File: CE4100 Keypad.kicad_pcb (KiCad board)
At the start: 2 copper layers, 114 x 152 mm, 54 parts, among them J1 USB_C, J2 AVR-ISP, J3 GU112X16G-7003, SW1 RESET, SW10 Key_1, SW11 Key_0, SW12 Key_Slash, SW13 Key_8, SW14 Key_5, SW15 Key_2, SW16 Key_Star, SW17 Key_9, SW18 Key_6, SW19 Key_3, SW2 Key_M1, SW20 Key_Del, SW21 Key_Minus, SW22 Key_Plus, SW23 Rotary_Switch, SW24 Key_Return, SW25 Rotary_Switch, SW3 Key_M2, SW4 Key_M3, SW5 Key_M4, SW6 Key_M5, SW7 Key_NumLock, SW8 Key_7, SW9 Key_4, U1 ATmega32U4

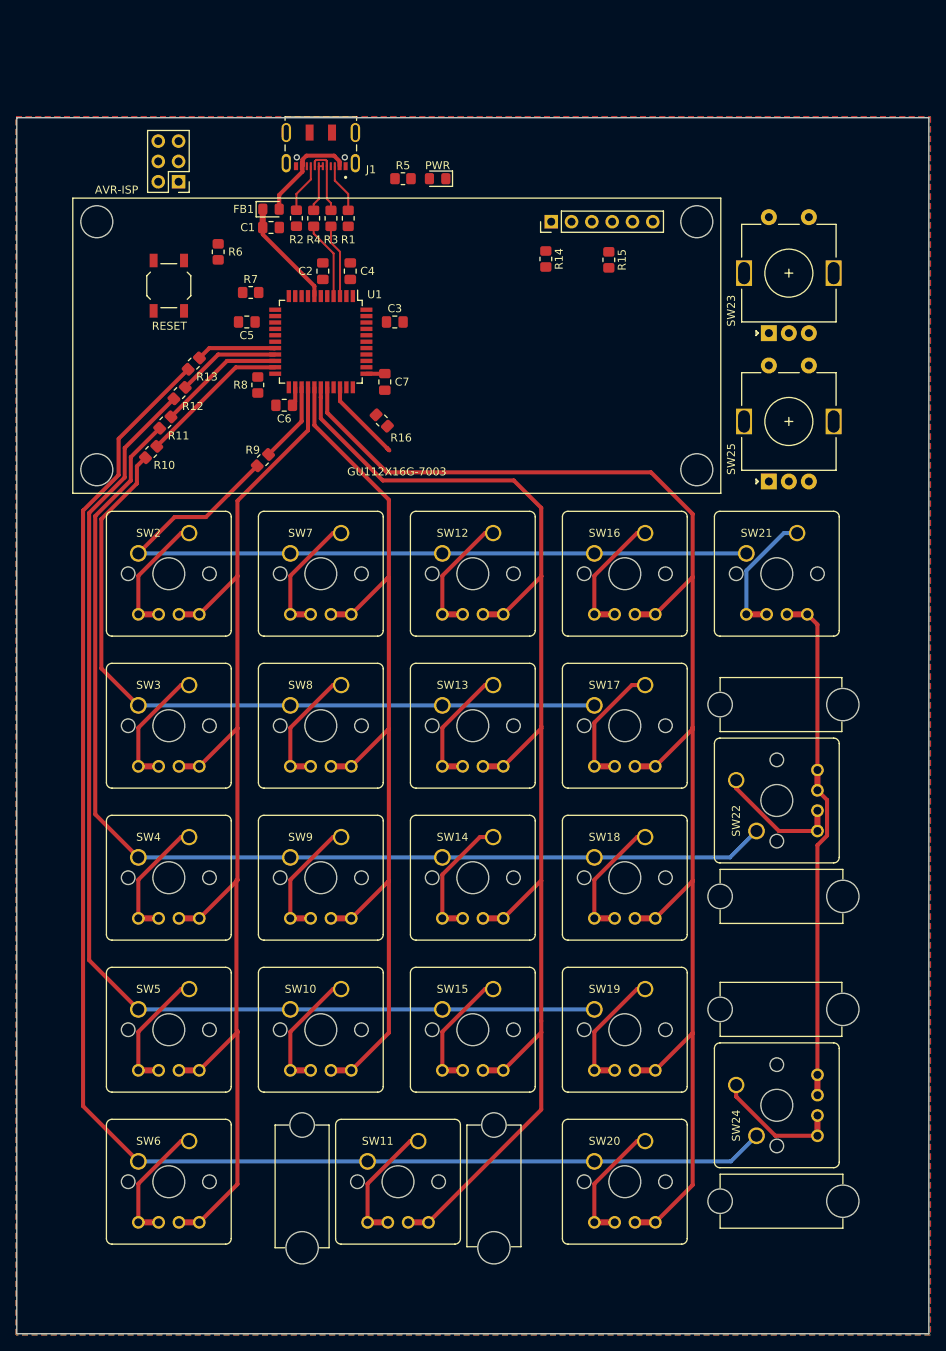
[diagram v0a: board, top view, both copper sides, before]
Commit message: Added more 3D models and worked on layout
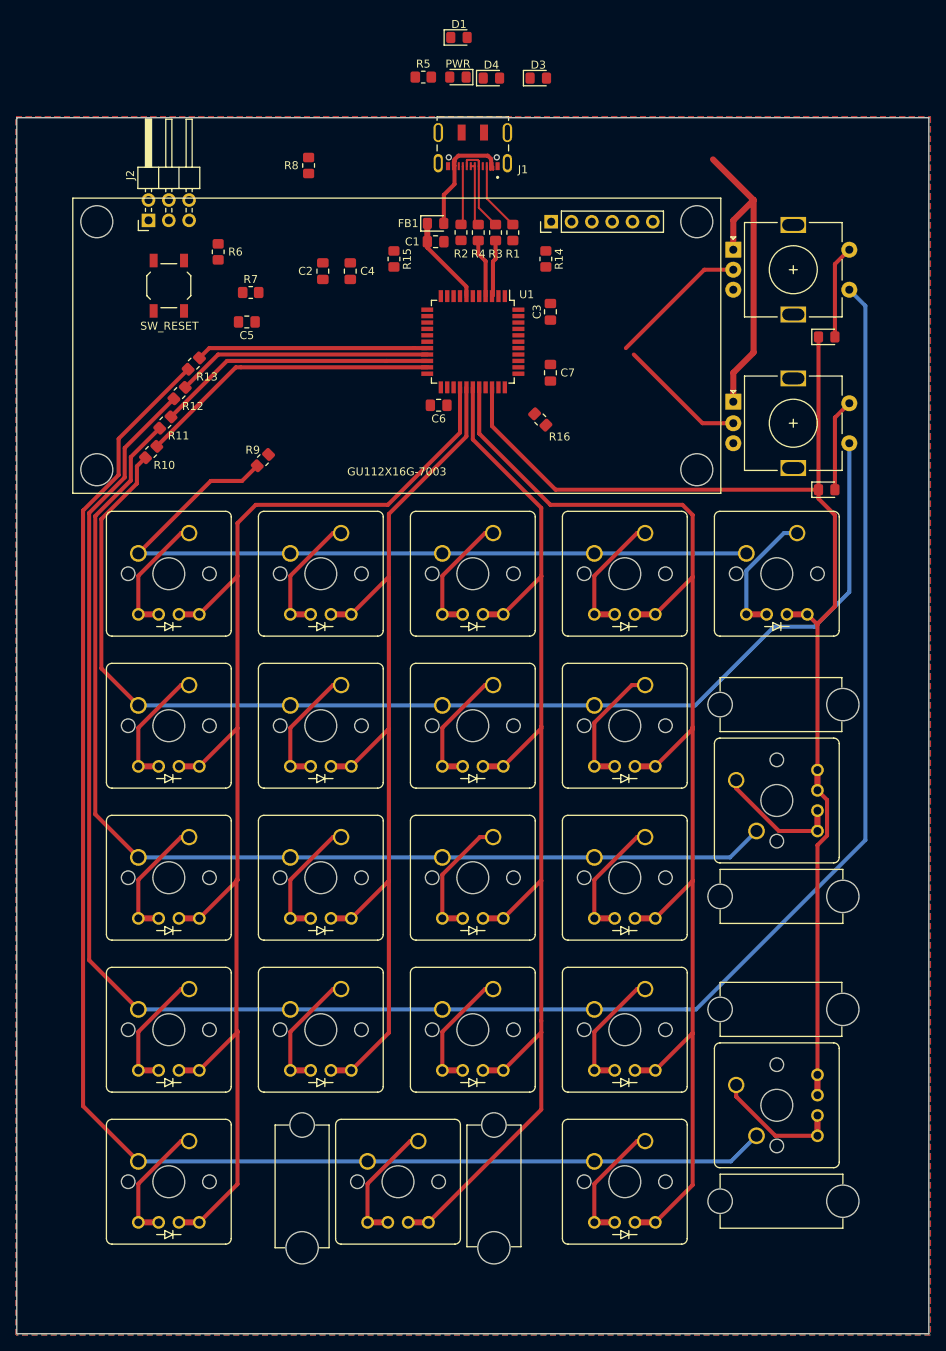
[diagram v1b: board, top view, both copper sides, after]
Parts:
- added D1: MBR120, Diode_SMD:D_0805_2012Metric_Pad1.15x1.40mm_HandSolder, F.Cu at (128.3, 14.0)
- added D3: RXLED, LED_SMD:LED_0805_2012Metric_Pad1.15x1.40mm_HandSolder, F.Cu at (138.2, 19.1)
- added D4: TXLED, LED_SMD:LED_0805_2012Metric_Pad1.15x1.40mm_HandSolder, F.Cu at (132.3, 19.1)
- added D5: 1N4148, Diode_SMD:D_0805_2012Metric_Pad1.15x1.40mm_HandSolder, F.Cu at (174.2, 51.4)
- added D6: 1N4148, Diode_SMD:D_0805_2012Metric_Pad1.15x1.40mm_HandSolder, F.Cu at (174.2, 70.5)
- J2: footprint Connector_PinHeader_2.54mm:PinHeader_2x03_P2.54mm_Vertical -> Connector_PinHeader_2.54mm:PinHeader_2x03_P2.54mm_Horizontal
- SW1: value RESET -> SW_RESET
- moved R8 28.2 mm to (109.5, 30.0)
- moved R15 26.9 mm to (120.1, 41.7)
- moved C7 20.7 mm to (139.7, 55.9)
- moved R3 20.7 mm to (132.8, 38.4)
- moved C1 20.7 mm to (125.3, 39.5)
- moved FB1 20.7 mm to (125.3, 37.2)
- moved R1 20.7 mm to (135.0, 38.4)
- moved R2 20.7 mm to (128.5, 38.3)
- moved R4 20.7 mm to (130.7, 38.4)
- moved R16 19.8 mm to (138.4, 61.7)
- moved C3 19.5 mm to (139.7, 48.3), turned to 90 degrees
- moved C6 19.3 mm to (125.7, 59.9)
- moved J1 19.0 mm to (130.0, 29.0)
- moved U1 19.0 mm to (130.0, 52.0)
- moved D2 13.0 mm to (128.1, 18.9)
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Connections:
- SW23 pad S1: Net-(R10-Pad1) -> Net-(R12-Pad1)
- SW23 pad S2: /COL4 -> Net-(D5-Pad2)
- SW25 pad S1: Net-(R12-Pad1) -> Net-(R10-Pad1)
- SW25 pad S2: /COL4 -> Net-(D6-Pad2)
- U1 pad 37: Net-(U1-Pad37) -> /KNOB2
- U1 pad 38: Net-(U1-Pad38) -> /KNOB1
- U1 pad 40: /KNOB2 -> Net-(U1-Pad40)
- U1 pad 41: /KNOB1 -> Net-(U1-Pad41)
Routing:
- net Net-(R12-Pad1): track 140.3 -> 252.5 mm
- net /COL4: track 75.0 -> 150.8 mm
- net Net-(R10-Pad1): track 92.2 -> 148.5 mm
- net +5V: track 4.09 -> 40.7 mm
- net /ROW1: track 18.9 -> 37.9 mm
- net /ROW3: track 13.0 -> 32.0 mm
- net /ROW2: track 15.9 -> 34.9 mm
- net /ROW4: track 10.1 -> 29.0 mm
- net /COL3: track 183.9 -> 166.4 mm
- net /COL0: track 149.9 -> 167.5 mm
- net /KNOB1: track 0.00 -> 17.5 mm
- net /COL2: track 171.1 -> 153.6 mm
- net /KNOB2: track 0.00 -> 16.0 mm
- net Net-(D5-Pad2): track 0.00 -> 11.6 mm
- net Net-(D6-Pad2): track 0.00 -> 11.6 mm
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
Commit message: Finished design and layout
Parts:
- removed R14, R15: 100, Resistor_SMD:R_0805_2012Metric_Pad1.20x1.40mm_HandSolder
- added C8: 100nF, Capacitor_SMD:C_0805_2012Metric_Pad1.18x1.45mm_HandSolder, F.Cu at (120.8, 49.3)
- added D10: 1N4148_SMD, Diode_SMD:D_SOD-123, F.Cu at (111.0, 109.5)
- added D11: 1N4148_SMD, Diode_SMD:D_SOD-123, F.Cu at (111.0, 128.5)
- added D12: 1N4148_SMD, Diode_SMD:D_SOD-123, F.Cu at (115.1, 147.5)
- added D13: 1N4148_SMD, Diode_SMD:D_SOD-123, F.Cu at (130.0, 90.5)
- added D14: 1N4148_SMD, Diode_SMD:D_SOD-123, F.Cu at (130.0, 109.5)
- added D15: 1N4148_SMD, Diode_SMD:D_SOD-123, F.Cu at (130.0, 128.5)
- added D16: 1N4148_SMD, Diode_SMD:D_SOD-123, F.Cu at (126.2, 147.5)
- added D17: 1N4148_SMD, Diode_SMD:D_SOD-123, F.Cu at (120.7, 166.5)
- added D18: 1N4148_SMD, Diode_SMD:D_SOD-123, F.Cu at (149.0, 90.5)
- added D19: 1N4148_SMD, Diode_SMD:D_SOD-123, F.Cu at (149.0, 109.5)
- added D20: 1N4148_SMD, Diode_SMD:D_SOD-123, F.Cu at (149.0, 128.5)
- added D21: 1N4148_SMD, Diode_SMD:D_SOD-123, F.Cu at (149.0, 147.5)
- added D22: 1N4148_SMD, Diode_SMD:D_SOD-123, F.Cu at (149.0, 166.5)
- added D23: 1N4148_SMD, Diode_SMD:D_SOD-123, F.Cu at (168.0, 90.5)
- added D24: 1N4148_SMD, Diode_SMD:D_SOD-123, F.Cu at (177.5, 109.5)
- added D25: 1N4148_SMD, Diode_SMD:D_SOD-123, F.Cu at (177.5, 147.5)
- added D26: 1N4148_THT, Diode_THT:D_DO-35_SOD27_P7.62mm_Horizontal, F.Cu at (180.0, 48.1)
- added D27: 1N4148_SMD, Diode_SMD:D_SOD-123, F.Cu at (182.5, 44.3)
- added D28: 1N4148_THT, Diode_THT:D_DO-35_SOD27_P7.62mm_Horizontal, F.Cu at (180.0, 67.3)
- added D29: 1N4148_SMD, Diode_SMD:D_SOD-123, F.Cu at (182.5, 63.5)
- added D7: 1N4148_SMD, Diode_SMD:D_SOD-123, F.Cu at (92.0, 147.5)
- added D8: 1N4148_SMD, Diode_SMD:D_SOD-123, F.Cu at (92.0, 166.5)
- added D9: 1N4148_SMD, Diode_SMD:D_SOD-123, F.Cu at (111.0, 90.5)
- added G1: LOGO, Silkscreen:MSOE, F.Cu at (150.5, 54.0)
- added H1: MountingHole, MountingHole:MountingHole_3.2mm_M3_Pad, F.Cu at (81.0, 30.0)
- added H2: MountingHole, MountingHole:MountingHole_3.2mm_M3_Pad, F.Cu at (179.0, 30.0)
- added H3: MountingHole, MountingHole:MountingHole_3.2mm_M3_Pad, F.Cu at (81.0, 168.0)
- added H4: MountingHole, MountingHole:MountingHole_3.2mm_M3_Pad, F.Cu at (179.0, 168.0)
- added Y1: 16MHz, CSTNE:CSTNE_Resonator, F.Cu at (117.1, 50.9)
- D1: value MBR120 -> PWR; footprint Diode_SMD:D_0805_2012Metric_Pad1.15x1.40mm_HandSolder -> LED_SMD:LED_0805_2012Metric_Pad1.15x1.40mm_HandSolder
- D2: value PWR -> RX
- D3: value RXLED -> TX
- D4: value TXLED -> 1N4148_SMD; footprint LED_SMD:LED_0805_2012Metric_Pad1.15x1.40mm_HandSolder -> Diode_SMD:D_SOD-123
- D5, D6: value 1N4148 -> 1N4148_SMD; footprint Diode_SMD:D_0805_2012Metric_Pad1.15x1.40mm_HandSolder -> Diode_SMD:D_SOD-123
- J2: footprint Connector_PinHeader_2.54mm:PinHeader_2x03_P2.54mm_Horizontal -> Connector_IDC:IDC-Header_2x03_P2.54mm_Horizontal
- R10, R11, R12, R13, R5, R7, R8, R9: value 470 -> 330
- SW1: value SW_RESET -> RESET; footprint Button_Switch_SMD:SW_SPST_TL3342 -> FSM2JSMAA:FSM2JSMAA
- SW10, SW12, SW13, SW14, SW15, SW16, SW17, SW18, SW19, SW2, SW20, SW21, SW3, SW4, SW5, SW6, SW7, SW8, SW9: footprint Switch_Cherry:Cherry_MX_Generic -> Switch_Cherry:Cherry_MX_Diode
- SW11, SW22: footprint Switch_Cherry:Cherry_MX_Generic_1x2 -> Switch_Cherry:Cherry_MX_Diode_1x2
- SW23: renamed from SW24; footprint Switch_Cherry:Cherry_MX_Generic_1x2 -> Switch_Cherry:Cherry_MX_Diode_1x2
- moved D5 100.7 mm to (92.0, 109.5), turned to 180 degrees
- moved D6 100.6 mm to (92.0, 128.5), turned to 180 degrees
- moved D4 82.0 mm to (92.0, 90.5), turned to 180 degrees
- moved C5 37.1 mm to (138.8, 47.2), turned to 0 degrees
- moved R16 26.0 mm to (153.5, 40.5), turned to 180 degrees
- moved D3 22.7 mm to (118.8, 30.9), turned to 90 degrees
- moved R7 20.9 mm to (121.1, 36.8), turned to 270 degrees
- moved D1 20.6 mm to (116.5, 30.9), turned to 90 degrees
- moved C4 19.8 mm to (134.5, 44.1), turned to 0 degrees
- moved R5 19.3 mm to (116.5, 36.8), turned to 270 degrees
- moved C2 18.4 mm to (129.7, 42.7), turned to 0 degrees
- moved SW1 16.5 mm to (108.1, 48.6), turned to 270 degrees
- moved C7 14.6 mm to (125.6, 59.8), turned to 180 degrees
- moved D2 13.9 mm to (121.1, 30.9), turned to 90 degrees
- moved C6 12.8 mm to (138.0, 56.3), turned to 90 degrees
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- renumbered SW23 to SW24
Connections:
- C1 pad 1: VBUS -> +5V
- D1 pad 1: +5V -> Net-(D1-Pad1)
- D1 pad 2: VBUS -> +5V
- D2 pad 1: GND -> Net-(D2-Pad1)
- D2 pad 2: Net-(D2-Pad2) -> +5V
- D4 pad 1: Net-(D4-Pad1) -> /COL0
- D4 pad 2: +5V -> Net-(D4-Pad2)
- D5 pad 1: /COL4 -> /COL0
- D6 pad 1: /COL4 -> /COL0
- FB1 pad 1: VBUS -> +5V
- J3 pad 2: Net-(J3-Pad2) -> /VFD_SIN
- J3 pad 4: /SBUSY -> /VFD_SBUSY
- J3 pad 5: Net-(J3-Pad5) -> /VFD_SCK
- R5 pad 1: +5V -> Net-(D1-Pad1)
- R5 pad 2: Net-(D2-Pad2) -> GND
- R7 pad 1: Net-(D3-Pad1) -> Net-(D2-Pad1)
- R8 pad 1: Net-(D4-Pad1) -> Net-(D3-Pad1)
- SW2 pad 2: Net-(SW2-Pad2) -> Net-(D4-Pad2)
- SW2 pad 3: Net-(SW2-Pad2) -> Net-(D4-Pad2)
- SW22 pad 1: Net-(R11-Pad1) -> Net-(R12-Pad1)
- SW24 pad S1: Net-(R12-Pad1) -> Net-(R10-Pad1)
- SW24 pad S2: Net-(D5-Pad2) -> Net-(D26-Pad2)
- SW25 pad S1: Net-(R10-Pad1) -> Net-(R11-Pad1)
- SW25 pad S2: Net-(D6-Pad2) -> Net-(D28-Pad2)
- SW3 pad 2: Net-(SW3-Pad2) -> Net-(D5-Pad2)
- SW3 pad 3: Net-(SW3-Pad2) -> Net-(D5-Pad2)
- SW4 pad 2: Net-(SW4-Pad2) -> Net-(D6-Pad2)
- SW4 pad 3: Net-(SW4-Pad2) -> Net-(D6-Pad2)
- U1 pad 1: /SBUSY -> Net-(U1-Pad1)
- U1 pad 32: /VFD_~RST -> Net-(U1-Pad32)
- U1 pad 36: Net-(U1-Pad36) -> /KNOB2
- U1 pad 37: /KNOB2 -> /KNOB1
- U1 pad 38: /KNOB1 -> /VFD_~RST
- U1 pad 39: Net-(U1-Pad39) -> /VFD_SCK
- U1 pad 40: Net-(U1-Pad40) -> /VFD_SBUSY
- U1 pad 41: Net-(U1-Pad41) -> /VFD_SIN
- U1 pad 7: VBUS -> +5V
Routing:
- net +5V: track 40.7 -> 182.0 mm
- net Net-(R12-Pad1): track 252.5 -> 172.1 mm
- net /COL4: track 150.8 -> 199.3 mm
- net Net-(R11-Pad1): track 137.9 -> 178.8 mm
- net GND: track 0.00 -> 38.1 mm, vias 0 -> 12
- net /MOSI: track 0.00 -> 33.6 mm
- net /MISO: track 0.00 -> 31.6 mm
- net /~RESET: track 0.00 -> 31.2 mm, vias 0 -> 1
- net /SCK: track 0.00 -> 30.9 mm
- net /ROW0: track 0.00 -> 30.5 mm
- net /VFD_~RST: track 0.00 -> 26.0 mm
- net /VFD_SCK: track 0.00 -> 24.1 mm
- net Net-(R8-Pad2): track 0.00 -> 23.7 mm, vias 0 -> 2
- net /VFD_SBUSY: track 0.00 -> 22.1 mm
- net Net-(D4-Pad2): track 0.00 -> 20.4 mm
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- removed copper zone on F.Cu, net GND
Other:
- board size 114 x 152 mm -> 108 x 148 mm
- board text added: "CE4100 Keypad Designed by Cody Nettesheim"
